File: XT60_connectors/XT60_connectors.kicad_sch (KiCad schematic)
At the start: 51 parts, among them J1 XT60-F, J10 XT60-F, J11 XT60-F, J2 XT60-F, J3 XT60_M, J4 XT60-F, J5 XT60-F, J6 XT60-F, J7 XT60-F, J8 XT60-F, J9 XT60-F

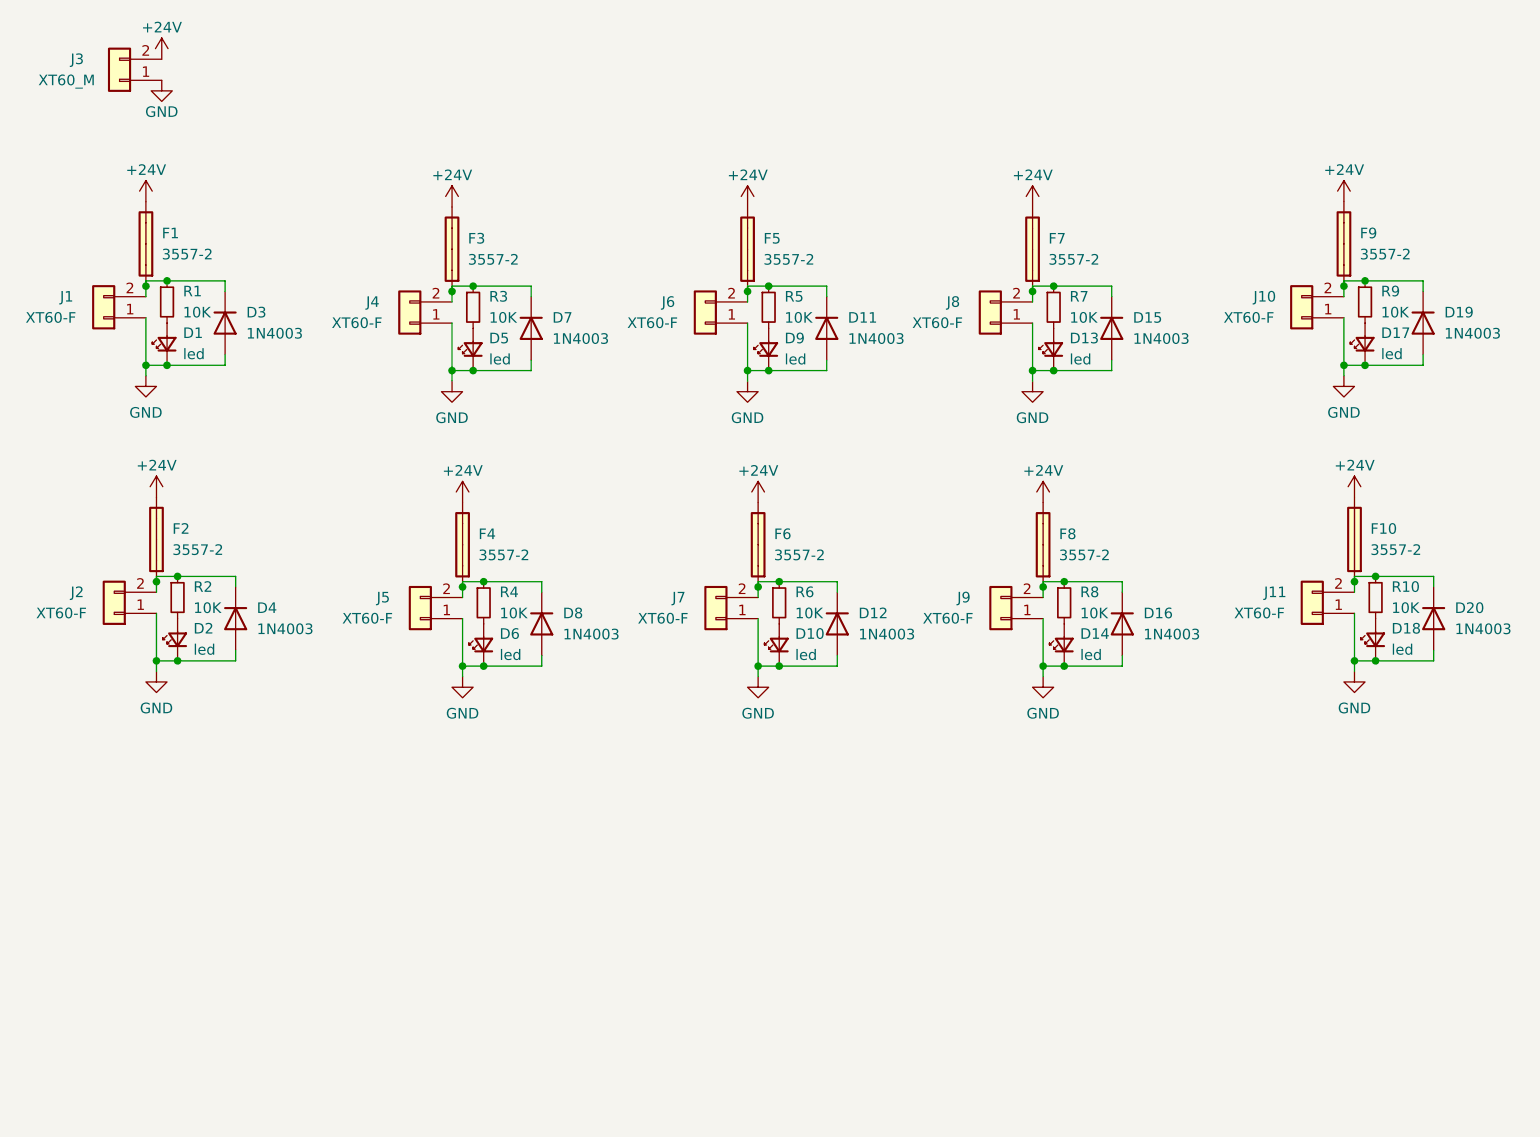
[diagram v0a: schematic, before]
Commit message: power connector added
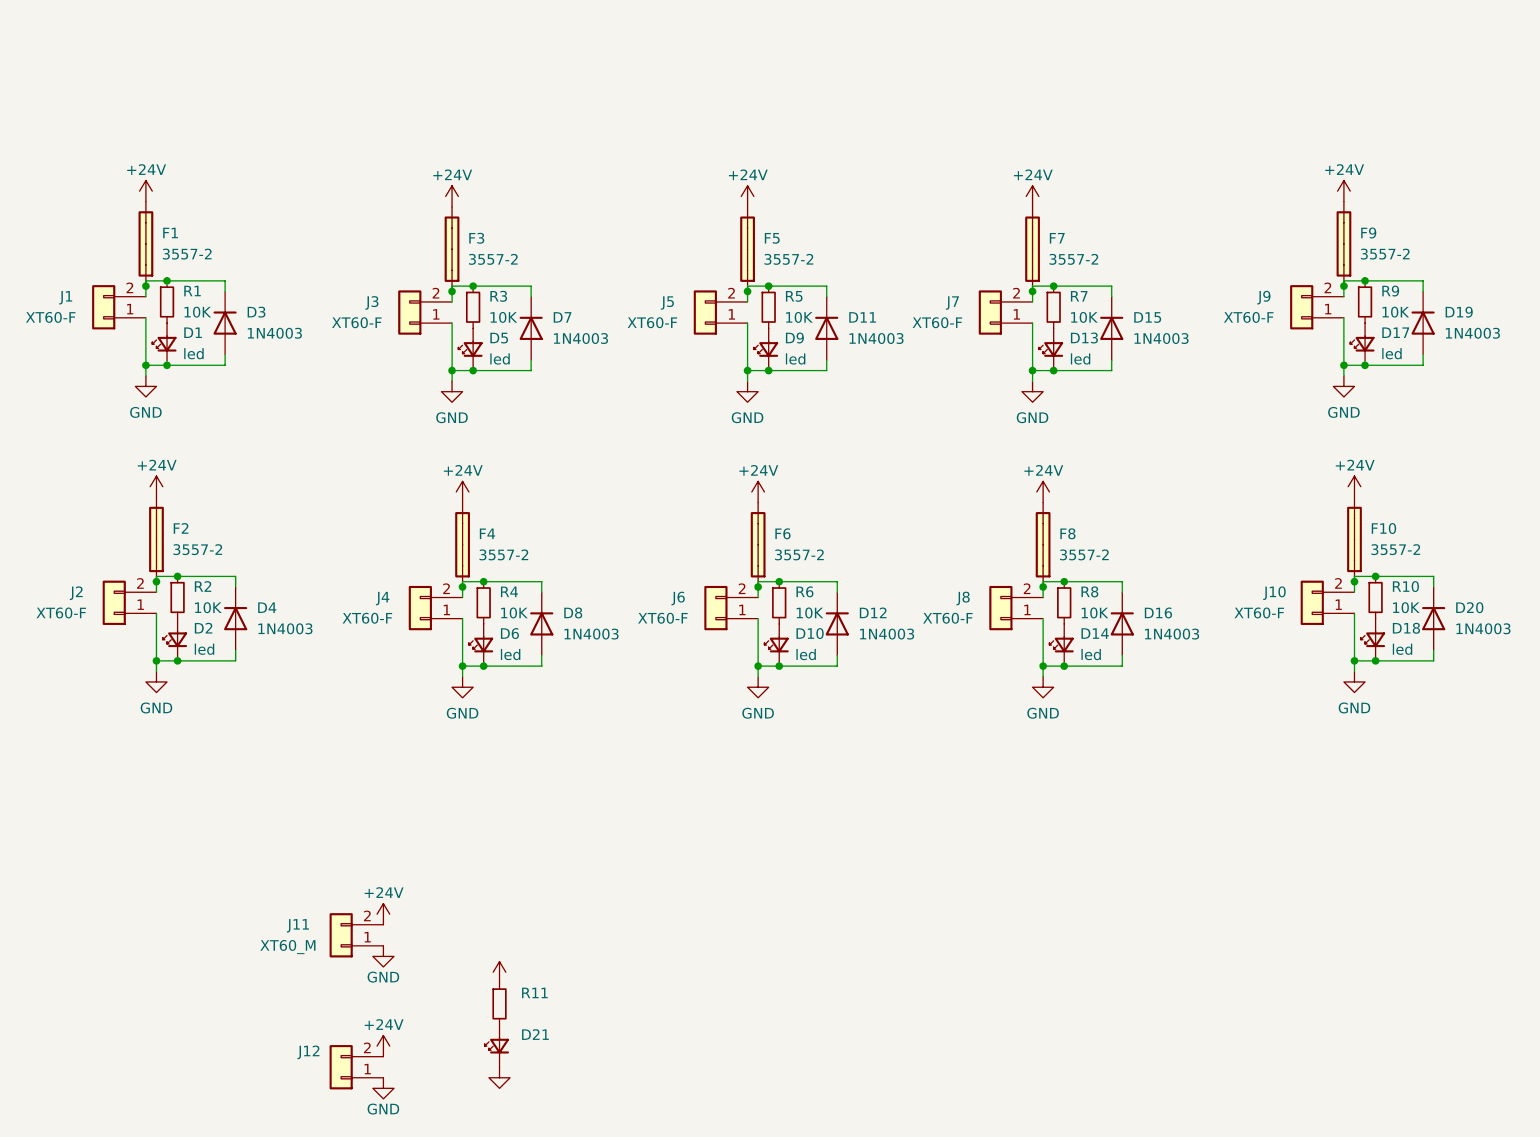
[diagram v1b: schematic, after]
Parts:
- removed J3: XT60_M, Connector_AMASS:AMASS_XT60-M_1x02_P7.20mm_Vertical, symbol Connector_Generic:Conn_01x02
- added D21: (no value), symbol Device:LED_Small
- added J11: XT60_M, Connector_AMASS:AMASS_XT60-M_1x02_P7.20mm_Vertical, symbol Connector_Generic:Conn_01x02
- added J12: (no value), symbol Connector_Generic:Conn_01x02
- added R11: (no value), symbol Device:R_Small
- renumbered J11 to J10, J4 to J3, J5 to J4, J6 to J5, J7 to J6, J8 to J7, J9 to J8, J10 to J9
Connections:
- net +24V: now also J11.2 (Pin_2), J12.2 (Pin_2), R11.1
- net GND: now also D21.1 (K), J11.1 (Pin_1), J12.1 (Pin_1)
- new net: D21.2 (A), R11.2
